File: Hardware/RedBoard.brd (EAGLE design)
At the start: 68.6 x 54.4 mm, 65 parts, among them IC3 LM1117, J1 POWER_JACKOVERPASTE_REDBOARD_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, J2 ICSP, Q1 ZXMP6A13FTA, Q2 2N7002PW, U1 FT231XS, U2 MIC5205, U3 ATMEGA328, Y1 16MHz

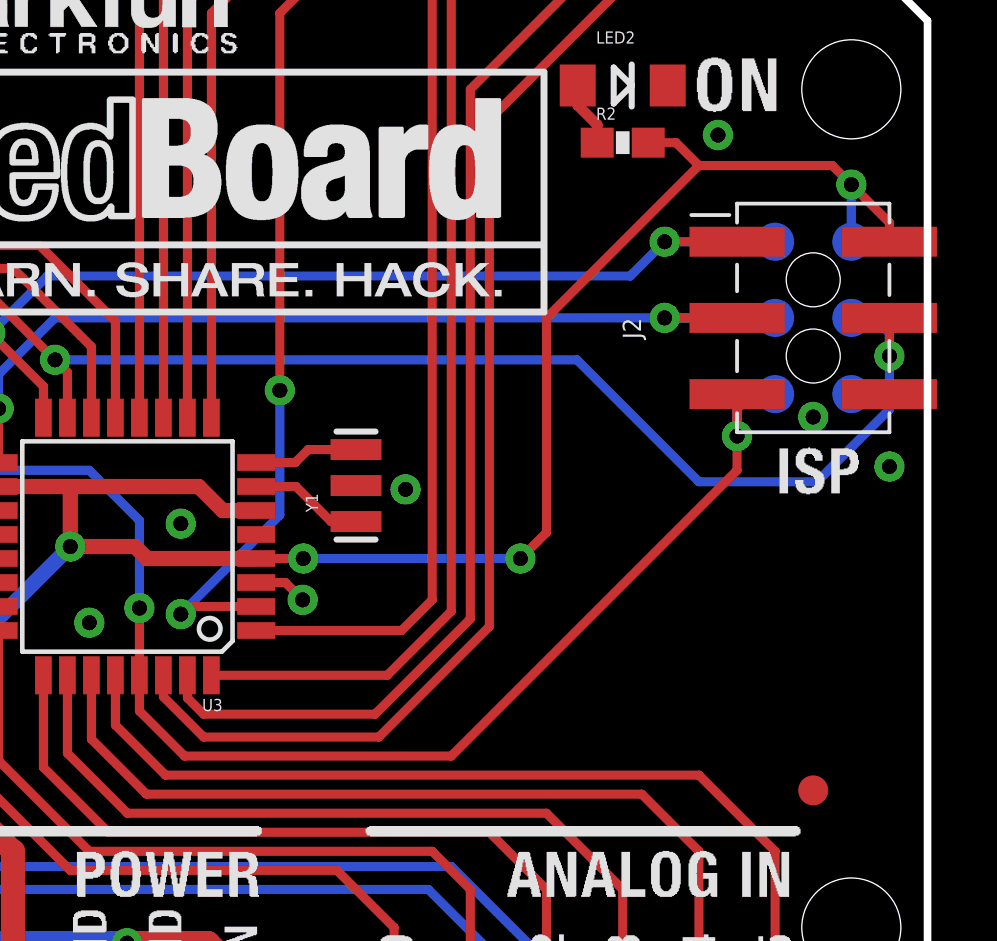
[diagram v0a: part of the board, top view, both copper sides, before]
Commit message: Tailing in ISP header pins
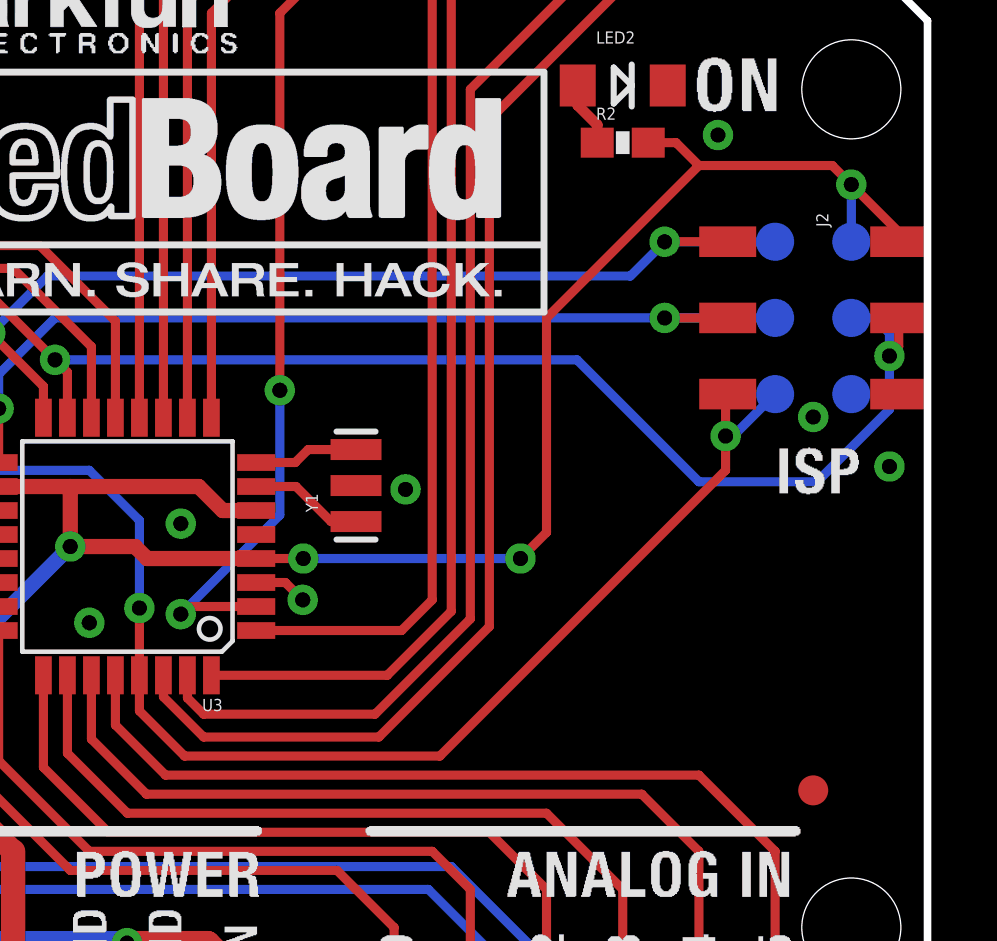
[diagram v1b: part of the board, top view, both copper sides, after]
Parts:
- J2: device SparkFun-Connectors:2X3_SMT_POSTS -> SparkFun-Connectors:2X3_SMD
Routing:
- net RESET: track 120.6 -> 119.4 mm
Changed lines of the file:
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@@
 <layer number="47" name="Measures" color="7" fill="1" visible="no" active="yes"/>
 <layer number="48" name="Document" color="7" fill="1" visible="no" active="yes"/>
-<layer number="49" name="ReferenceLC" color="13" fill="1" visible="yes" active="yes"/>
+<layer number="49" name="ReferenceLC" color="13" fill="1" visible="no" active="yes"/>
 <layer number="50" name="ReferenceLS" color="12" fill="1" visible="no" active="yes"/>
 <layer number="51" name="tDocu" color="6" fill="1" visible="yes" active="yes"/>
@@
 <element name="JP1" library="SparkFun-Aesthetics" package="SFE-NEW-WEB" value="LOGO-SFENW2" x="33.0454" y="37.211"/>
 <element name="JP7" library="SparkFun-Aesthetics" package="SFE-LOGO-FLAME" value="LOGO-SFESK" x="40.0304" y="39.878"/>
-<element name="J2" library="SparkFun-Connectors" package="2X3_SMT_POSTS" value="ICSP" x="64.77" y="28.448" rot="R270"/>
+<element name="J2" library="SparkFun-Connectors" package="2X3_SMD" value="ICSP" x="64.77" y="28.448" rot="R270"/>
 <element name="C6" library="SparkFun" package="EIA3216" value="10uF" x="20.32" y="22.86"/>
 <element name="U1" library="SparkFun-DigitalIC" package="SSOP20_L" value="FT231XS" x="17.78" y="39.37" rot="R180"/>
@@
 <contactref element="TP2" pad="P$1"/>
 <via x="67.31" y="27.178" extent="1-16" drill="0.508"/>
-<wire x1="67.31" y1="28.448" x2="67.31" y2="27.178" width="0.3048" layer="1"/>
 <wire x1="66.04" y1="28.448" x2="66.802" y2="28.448" width="0.3048" layer="16"/>
 <wire x1="66.802" y1="28.448" x2="67.31" y2="27.94" width="0.3048" layer="16"/>
@@
 <wire x1="67.31" y1="27.178" x2="67.31" y2="25.4" width="0.3048" layer="16"/>
 <wire x1="64.897" y1="22.987" x2="67.31" y2="25.4" width="0.3048" layer="16"/>
+<wire x1="67.62" y1="28.448" x2="67.62" y2="27.488" width="0.3048" layer="1"/>
+<wire x1="67.62" y1="27.488" x2="67.31" y2="27.178" width="0.3048" layer="1"/>
 </signal>
 <signal name="MISO">
@@
 <wire x1="59.817" y1="30.988" x2="58.674" y2="29.845" width="0.3048" layer="16"/>
 <via x="59.817" y="30.988" extent="1-16" drill="0.508"/>
-<wire x1="59.817" y1="30.988" x2="62.23" y2="30.988" width="0.3048" layer="1"/>
+<wire x1="59.817" y1="30.988" x2="61.92" y2="30.988" width="0.3048" layer="1"/>
 <wire x1="63.5" y1="30.988" x2="59.817" y2="30.988" width="0.3048" layer="16"/>
 </signal>
@@
 <wire x1="39.497" y1="28.448" x2="59.817" y2="28.448" width="0.3048" layer="16"/>
 <via x="59.817" y="28.448" extent="1-16" drill="0.508"/>
-<wire x1="59.817" y1="28.448" x2="62.23" y2="28.448" width="0.3048" layer="1"/>
+<wire x1="59.817" y1="28.448" x2="61.92" y2="28.448" width="0.3048" layer="1"/>
 <wire x1="63.5" y1="28.448" x2="59.817" y2="28.448" width="0.3048" layer="16"/>
 </signal>
@@
 <wire x1="66.04" y1="30.988" x2="66.04" y2="32.893" width="0.3048" layer="16"/>
 <wire x1="65.405" y1="33.528" x2="66.04" y2="32.893" width="0.3048" layer="1"/>
-<wire x1="67.31" y1="30.988" x2="67.31" y2="31.623" width="0.3048" layer="1"/>
-<wire x1="67.31" y1="31.623" x2="66.04" y2="32.893" width="0.3048" layer="1"/>
+<wire x1="67.62" y1="31.313" x2="66.04" y2="32.893" width="0.3048" layer="1"/>
+<wire x1="67.62" y1="30.988" x2="67.62" y2="31.313" width="0.3048" layer="1"/>
 </signal>
 <signal name="GND">
@@
 <contactref element="U3" pad="29"/>
 <wire x1="42.31" y1="15.348" x2="43.815" y2="13.843" width="0.3048" layer="1"/>
-<wire x1="43.815" y1="13.843" x2="52.705" y2="13.843" width="0.3048" layer="1"/>
+<wire x1="43.815" y1="13.843" x2="52.324" y2="13.843" width="0.3048" layer="1"/>
 <wire x1="33.02" y1="4.698" x2="33.02" y2="23.368" width="0.3048" layer="1"/>
 <wire x1="42.31" y1="18.777" x2="42.31" y2="16.5354" width="0.3048" layer="1"/>
@@
 <wire x1="33.02" y1="1.398" x2="33.02" y2="4.698" width="0.3048" layer="1"/>
 <contactref element="J2" pad="5"/>
-<wire x1="62.23" y1="25.908" x2="62.992" y2="25.908" width="0.3048" layer="1"/>
 <wire x1="12.7" y1="48.26" x2="12.7" y2="36.83" width="0.3048" layer="16"/>
 <wire x1="12.7" y1="36.83" x2="22.86" y2="26.67" width="0.3048" layer="16"/>
 <wire x1="28.79" y1="27.94" x2="28.79" y2="29.845" width="0.3048" layer="1"/>
 <contactref element="TP6" pad="P$1"/>
-<via x="62.23" y="24.511" extent="1-16" drill="0.508"/>
+<via x="61.849" y="24.511" extent="1-16" drill="0.508"/>
 <wire x1="22.86" y1="26.67" x2="28.79" y2="26.67" width="0.3048" layer="16"/>
 <via x="28.79" y="26.67" extent="1-16" drill="0.508"/>
@@
 <wire x1="29.718" y1="26.67" x2="28.79" y2="26.67" width="0.3048" layer="1"/>
 <wire x1="28.79" y1="27.94" x2="28.79" y2="26.67" width="0.3048" layer="1"/>
-<wire x1="62.23" y1="23.368" x2="62.23" y2="24.511" width="0.3048" layer="1"/>
-<wire x1="52.705" y1="13.843" x2="62.23" y2="23.368" width="0.3048" layer="1"/>
-<wire x1="62.23" y1="24.511" x2="62.23" y2="25.908" width="0.3048" layer="1"/>
-<wire x1="63.5" y1="25.908" x2="62.738" y2="25.908" width="0.3048" layer="16"/>
-<wire x1="62.738" y1="25.908" x2="62.23" y2="25.4" width="0.3048" layer="16"/>
-<wire x1="62.23" y1="25.4" x2="62.23" y2="24.511" width="0.3048" layer="16"/>
+<wire x1="61.849" y1="23.368" x2="61.849" y2="24.511" width="0.3048" layer="1"/>
+<wire x1="61.849" y1="24.511" x2="61.849" y2="25.837" width="0.3048" layer="1"/>
+<wire x1="61.849" y1="25.837" x2="61.92" y2="25.908" width="0.3048" layer="1"/>
+<wire x1="63.5" y1="25.908" x2="62.103" y2="24.511" width="0.3048" layer="16"/>
+<wire x1="62.103" y1="24.511" x2="61.849" y2="24.511" width="0.3048" layer="16"/>
+<wire x1="52.324" y1="13.843" x2="61.849" y2="23.368" width="0.3048" layer="1"/>
 </signal>
 <signal name="AREF">

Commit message: Back to old ISP. Tucked in the paste on edge pins
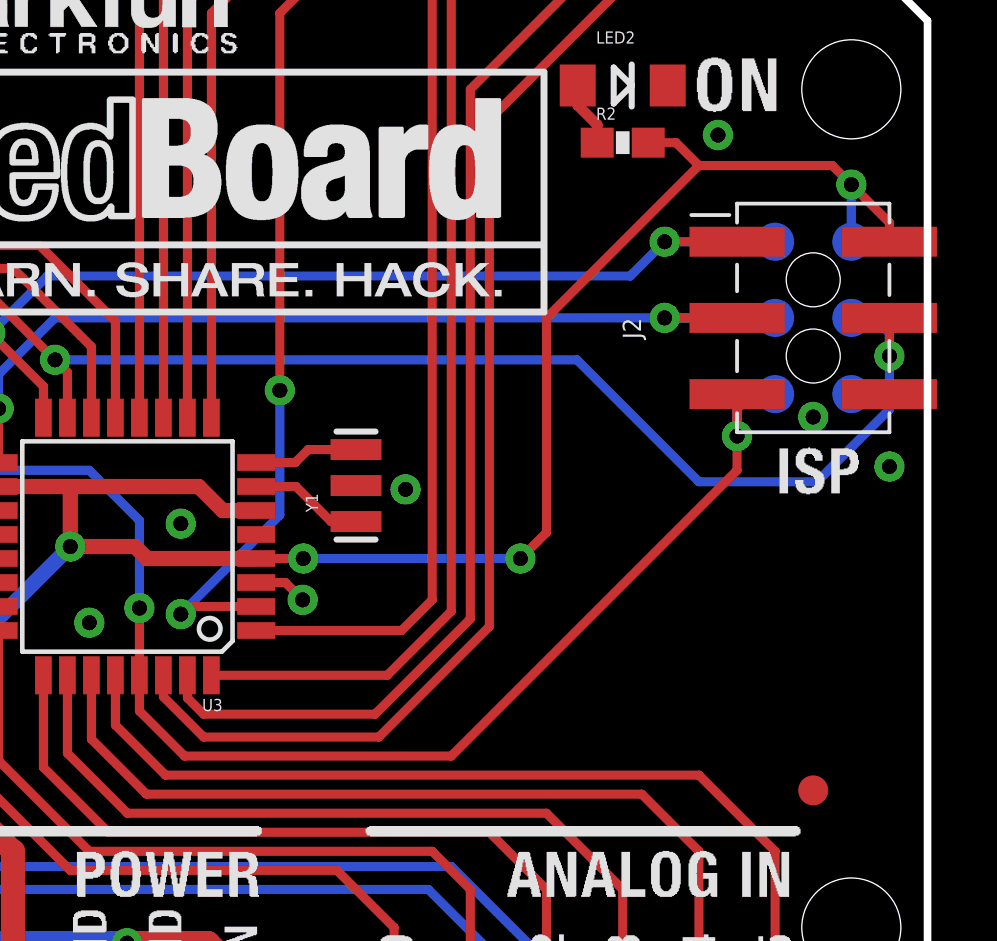
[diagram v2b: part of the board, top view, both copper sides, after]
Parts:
- J2: device SparkFun-Connectors:2X3_SMD -> SparkFun-Connectors:2X3_SMT_POSTS
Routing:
- net RESET: track 119.4 -> 120.6 mm
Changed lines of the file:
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@@
 <layer number="29" name="tStop" color="2" fill="3" visible="no" active="yes"/>
 <layer number="30" name="bStop" color="5" fill="6" visible="no" active="yes"/>
-<layer number="31" name="tCream" color="7" fill="4" visible="no" active="yes"/>
+<layer number="31" name="tCream" color="7" fill="4" visible="yes" active="yes"/>
 <layer number="32" name="bCream" color="7" fill="5" visible="no" active="yes"/>
 <layer number="33" name="tFinish" color="6" fill="3" visible="no" active="yes"/>
@@
 <layer number="47" name="Measures" color="7" fill="1" visible="no" active="yes"/>
 <layer number="48" name="Document" color="7" fill="1" visible="no" active="yes"/>
-<layer number="49" name="ReferenceLC" color="13" fill="1" visible="no" active="yes"/>
+<layer number="49" name="ReferenceLC" color="13" fill="1" visible="yes" active="yes"/>
 <layer number="50" name="ReferenceLS" color="12" fill="1" visible="no" active="yes"/>
 <layer number="51" name="tDocu" color="6" fill="1" visible="yes" active="yes"/>
@@
 <element name="JP1" library="SparkFun-Aesthetics" package="SFE-NEW-WEB" value="LOGO-SFENW2" x="33.0454" y="37.211"/>
 <element name="JP7" library="SparkFun-Aesthetics" package="SFE-LOGO-FLAME" value="LOGO-SFESK" x="40.0304" y="39.878"/>
-<element name="J2" library="SparkFun-Connectors" package="2X3_SMD" value="ICSP" x="64.77" y="28.448" rot="R270"/>
+<element name="J2" library="SparkFun-Connectors" package="2X3_SMT_POSTS" value="ICSP" x="64.77" y="28.448" rot="R270"/>
 <element name="C6" library="SparkFun" package="EIA3216" value="10uF" x="20.32" y="22.86"/>
 <element name="U1" library="SparkFun-DigitalIC" package="SSOP20_L" value="FT231XS" x="17.78" y="39.37" rot="R180"/>
@@
 <contactref element="TP2" pad="P$1"/>
 <via x="67.31" y="27.178" extent="1-16" drill="0.508"/>
+<wire x1="67.31" y1="28.448" x2="67.31" y2="27.178" width="0.3048" layer="1"/>
 <wire x1="66.04" y1="28.448" x2="66.802" y2="28.448" width="0.3048" layer="16"/>
 <wire x1="66.802" y1="28.448" x2="67.31" y2="27.94" width="0.3048" layer="16"/>
@@
 <wire x1="67.31" y1="27.178" x2="67.31" y2="25.4" width="0.3048" layer="16"/>
 <wire x1="64.897" y1="22.987" x2="67.31" y2="25.4" width="0.3048" layer="16"/>
-<wire x1="67.62" y1="28.448" x2="67.62" y2="27.488" width="0.3048" layer="1"/>
-<wire x1="67.62" y1="27.488" x2="67.31" y2="27.178" width="0.3048" layer="1"/>
 </signal>
 <signal name="MISO">
@@
 <wire x1="59.817" y1="30.988" x2="58.674" y2="29.845" width="0.3048" layer="16"/>
 <via x="59.817" y="30.988" extent="1-16" drill="0.508"/>
-<wire x1="59.817" y1="30.988" x2="61.92" y2="30.988" width="0.3048" layer="1"/>
+<wire x1="59.817" y1="30.988" x2="62.23" y2="30.988" width="0.3048" layer="1"/>
 <wire x1="63.5" y1="30.988" x2="59.817" y2="30.988" width="0.3048" layer="16"/>
 </signal>
@@
 <wire x1="39.497" y1="28.448" x2="59.817" y2="28.448" width="0.3048" layer="16"/>
 <via x="59.817" y="28.448" extent="1-16" drill="0.508"/>
-<wire x1="59.817" y1="28.448" x2="61.92" y2="28.448" width="0.3048" layer="1"/>
+<wire x1="59.817" y1="28.448" x2="62.23" y2="28.448" width="0.3048" layer="1"/>
 <wire x1="63.5" y1="28.448" x2="59.817" y2="28.448" width="0.3048" layer="16"/>
 </signal>
@@
 <wire x1="66.04" y1="30.988" x2="66.04" y2="32.893" width="0.3048" layer="16"/>
 <wire x1="65.405" y1="33.528" x2="66.04" y2="32.893" width="0.3048" layer="1"/>
-<wire x1="67.62" y1="31.313" x2="66.04" y2="32.893" width="0.3048" layer="1"/>
-<wire x1="67.62" y1="30.988" x2="67.62" y2="31.313" width="0.3048" layer="1"/>
+<wire x1="67.31" y1="30.988" x2="67.31" y2="31.623" width="0.3048" layer="1"/>
+<wire x1="67.31" y1="31.623" x2="66.04" y2="32.893" width="0.3048" layer="1"/>
 </signal>
 <signal name="GND">
@@
 <contactref element="U3" pad="29"/>
 <wire x1="42.31" y1="15.348" x2="43.815" y2="13.843" width="0.3048" layer="1"/>
-<wire x1="43.815" y1="13.843" x2="52.324" y2="13.843" width="0.3048" layer="1"/>
+<wire x1="43.815" y1="13.843" x2="52.705" y2="13.843" width="0.3048" layer="1"/>
 <wire x1="33.02" y1="4.698" x2="33.02" y2="23.368" width="0.3048" layer="1"/>
 <wire x1="42.31" y1="18.777" x2="42.31" y2="16.5354" width="0.3048" layer="1"/>
@@
 <wire x1="33.02" y1="1.398" x2="33.02" y2="4.698" width="0.3048" layer="1"/>
 <contactref element="J2" pad="5"/>
+<wire x1="62.23" y1="25.908" x2="62.992" y2="25.908" width="0.3048" layer="1"/>
 <wire x1="12.7" y1="48.26" x2="12.7" y2="36.83" width="0.3048" layer="16"/>
 <wire x1="12.7" y1="36.83" x2="22.86" y2="26.67" width="0.3048" layer="16"/>
 <wire x1="28.79" y1="27.94" x2="28.79" y2="29.845" width="0.3048" layer="1"/>
 <contactref element="TP6" pad="P$1"/>
-<via x="61.849" y="24.511" extent="1-16" drill="0.508"/>
+<via x="62.23" y="24.511" extent="1-16" drill="0.508"/>
 <wire x1="22.86" y1="26.67" x2="28.79" y2="26.67" width="0.3048" layer="16"/>
 <via x="28.79" y="26.67" extent="1-16" drill="0.508"/>
@@
 <wire x1="29.718" y1="26.67" x2="28.79" y2="26.67" width="0.3048" layer="1"/>
 <wire x1="28.79" y1="27.94" x2="28.79" y2="26.67" width="0.3048" layer="1"/>
-<wire x1="61.849" y1="23.368" x2="61.849" y2="24.511" width="0.3048" layer="1"/>
-<wire x1="61.849" y1="24.511" x2="61.849" y2="25.837" width="0.3048" layer="1"/>
-<wire x1="61.849" y1="25.837" x2="61.92" y2="25.908" width="0.3048" layer="1"/>
-<wire x1="63.5" y1="25.908" x2="62.103" y2="24.511" width="0.3048" layer="16"/>
-<wire x1="62.103" y1="24.511" x2="61.849" y2="24.511" width="0.3048" layer="16"/>
-<wire x1="52.324" y1="13.843" x2="61.849" y2="23.368" width="0.3048" layer="1"/>
+<wire x1="62.23" y1="23.368" x2="62.23" y2="24.511" width="0.3048" layer="1"/>
+<wire x1="52.705" y1="13.843" x2="62.23" y2="23.368" width="0.3048" layer="1"/>
+<wire x1="62.23" y1="24.511" x2="62.23" y2="25.908" width="0.3048" layer="1"/>
+<wire x1="63.5" y1="25.908" x2="62.738" y2="25.908" width="0.3048" layer="16"/>
+<wire x1="62.738" y1="25.908" x2="62.23" y2="25.4" width="0.3048" layer="16"/>
+<wire x1="62.23" y1="25.4" x2="62.23" y2="24.511" width="0.3048" layer="16"/>
 </signal>
 <signal name="AREF">
